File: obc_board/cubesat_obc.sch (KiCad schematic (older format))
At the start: 0 parts

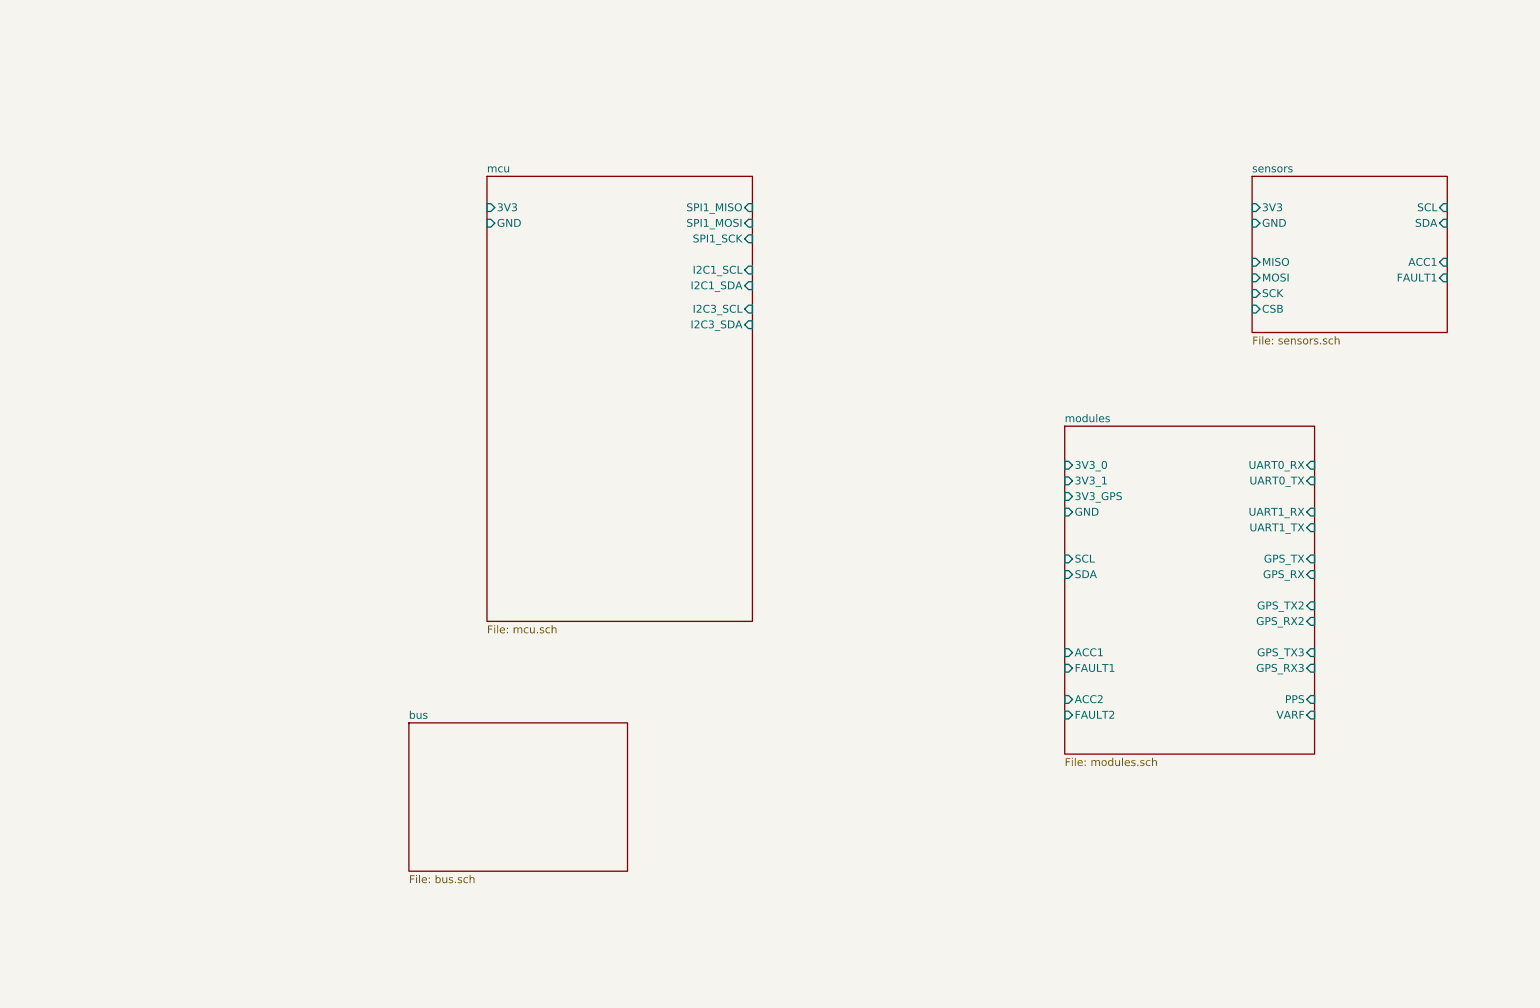
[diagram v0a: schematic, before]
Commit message: add memory
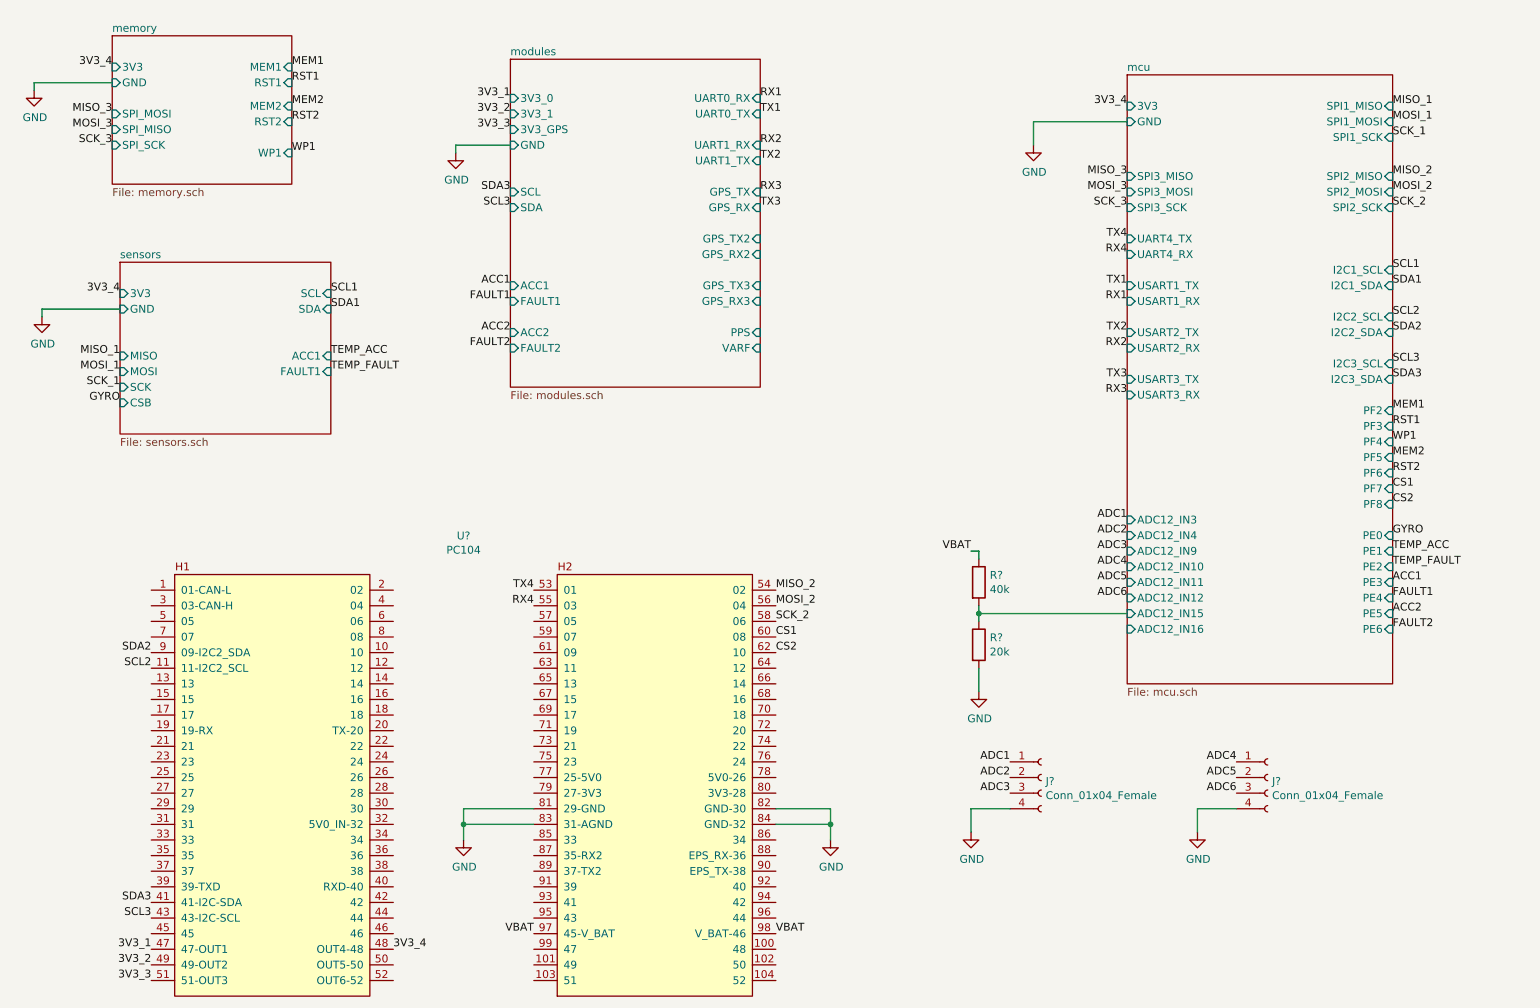
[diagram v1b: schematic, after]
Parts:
- added J? (x2): Conn_01x04_Female, symbol Connector:Conn_01x04_Female
- added R?: 40k, symbol Device:R
- added R?: 20k, symbol Device:R
- added U?: PC104, symbol cubesat_obc_lib:PC104
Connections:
- new net 3V3_1: U?.47 (47-OUT1)
- new net 3V3_2: U?.49 (49-OUT2)
- new net 3V3_3: U?.51 (51-OUT3)
- new net 3V3_4: U?.48 (OUT4-48)
- new net ADC1: J?.1 (Pin_1)
- new net ADC2: J?.2 (Pin_2)
- new net ADC3: J?.3 (Pin_3)
- new net ADC4: J?.1 (Pin_1)
- new net ADC5: J?.2 (Pin_2)
- new net ADC6: J?.3 (Pin_3)
- new net CS1: U?.60 (08)
- new net CS2: U?.62 (10)
- new net GND: J?.4 (Pin_4), J?.4 (Pin_4), R?.2, U?.81 (29-GND), U?.82 (GND-30), U?.83 (31-AGND), U?.84 (GND-32)
- new net MISO_2: U?.54 (02)
- new net MOSI_2: U?.56 (04)
- new net RX4: U?.55 (03)
- new net SCK_2: U?.58 (06)
- new net SCL2: U?.11 (11-I2C2_SCL)
- new net SCL3: U?.43 (43-I2C-SCL)
- new net SDA2: U?.9 (09-I2C2_SDA)
- new net SDA3: U?.41 (41-I2C-SDA)
- new net TX4: U?.53 (01)
- new net VBAT: R?.1, U?.97 (45-V_BAT), U?.98 (V_BAT-46)
- new net mcu/ADC12_IN15: R?.1, R?.2

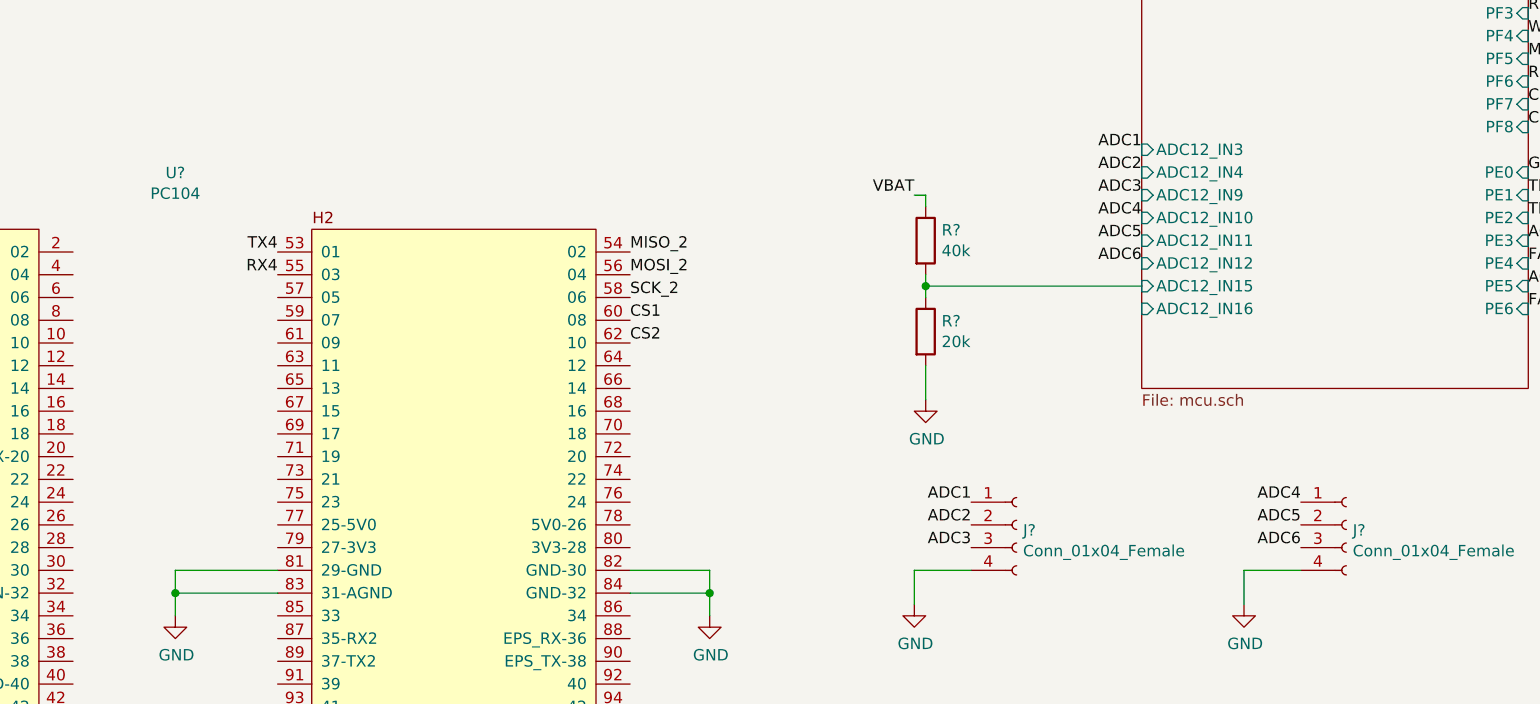
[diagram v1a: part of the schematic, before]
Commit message: updated footprints
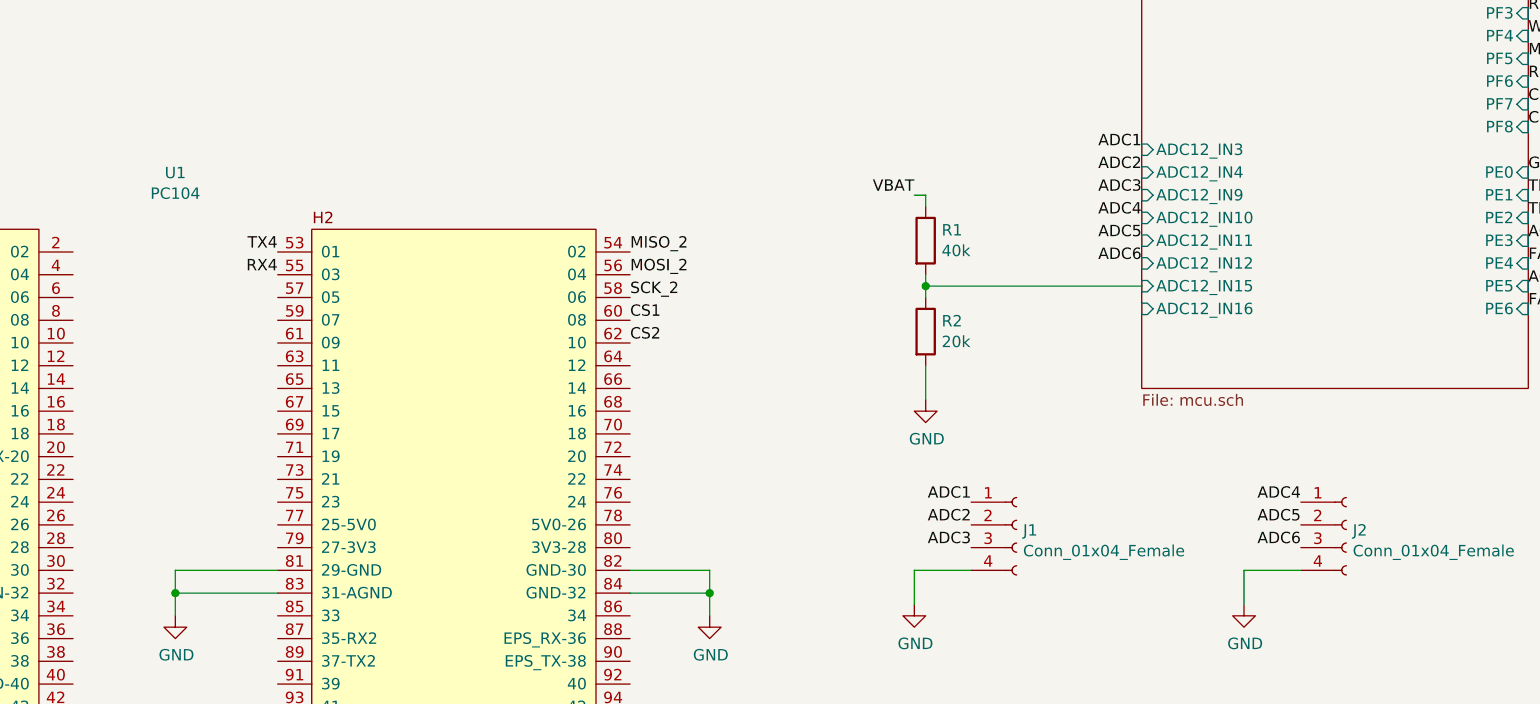
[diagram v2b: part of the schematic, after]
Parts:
- U1: renamed from U?; footprint (none) -> cubesat_obc:PC104-Standard; Digikey Part Number (none) -> 609-10153302-20111LF-ND
- gave numbers to parts that had none: 4
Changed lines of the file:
@@
 $EndDescr
 $Comp
-L power:GND #PWR?
+L power:GND #PWR0101
 U 1 1 5F33CD00
 P 7350 1750
-F 0 "#PWR?" H 7350 1500 50  0001 C CNN
+F 0 "#PWR0101" H 7350 1500 50  0001 C CNN
 F 1 "GND" H 7355 1577 50  0000 C CNN
 F 2 "" H 7350 1750 50  0001 C CNN
@@
 	7350 1750 7350 1600
 $Comp
-L power:GND #PWR?
+L power:GND #PWR0102
 U 1 1 5F33D036
 P 6050 6200
-F 0 "#PWR?" H 6050 5950 50  0001 C CNN
+F 0 "#PWR0102" H 6050 5950 50  0001 C CNN
 F 1 "GND" H 6055 6027 50  0000 C CNN
 F 2 "" H 6050 6200 50  0001 C CNN
@@
 	6050 6100 6050 6000
 $Comp
-L power:GND #PWR?
+L power:GND #PWR0103
 U 1 1 5F33D67B
 P 3700 6200
-F 0 "#PWR?" H 3700 5950 50  0001 C CNN
+F 0 "#PWR0103" H 3700 5950 50  0001 C CNN
 F 1 "GND" H 3705 6027 50  0000 C CNN
 F 2 "" H 3700 6200 50  0001 C CNN
@@
 	3700 6100 3700 6000
 $Comp
-L power:GND #PWR?
+L power:GND #PWR0104
 U 1 1 5F33E025
 P 3650 1800
-F 0 "#PWR?" H 3650 1550 50  0001 C CNN
+F 0 "#PWR0104" H 3650 1550 50  0001 C CNN
 F 1 "GND" H 3655 1627 50  0000 C CNN
 F 2 "" H 3650 1800 50  0001 C CNN
@@
 	3650 1750 3650 1800
 $Comp
-L power:GND #PWR?
+L power:GND #PWR0105
 U 1 1 5F33EB7E
 P 1000 2850
-F 0 "#PWR?" H 1000 2600 50  0001 C CNN
+F 0 "#PWR0105" H 1000 2600 50  0001 C CNN
 F 1 "GND" H 1005 2677 50  0000 C CNN
 F 2 "" H 1000 2850 50  0001 C CNN
@@
 3V3_4
 $Comp
-L cubesat_obc_lib:PC104 U?
+L cubesat_obc_lib:PC104 U1
 U 1 1 5F3402F4
 P 3700 5800
-F 0 "U?" H 3700 7348 50  0000 C CNN
+F 0 "U1" H 3700 7348 50  0000 C CNN
 F 1 "PC104" H 3700 7257 50  0000 C CNN
-F 2 "" H 2600 6600 50  0001 C CNN
-F 3 "" H 2600 6600 50  0001 C CNN
+F 2 "cubesat_obc:PC104-Standard" H 2600 6600 50  0001 C CNN
+F 3 "https://cdn.amphenol-icc.com/media/wysiwyg/files/drawing/10153302.pdf" H 2600 6600 50  0001 C CNN
+F 4 "	609-10153302-20111LF-ND" H 3700 5800 50  0001 C CNN "Digikey Part Number"
 	1    3700 5800
 	1    0    0    -1
@@
 RST2
 $Comp
-L power:GND #PWR?
+L power:GND #PWR0106
 U 1 1 5F5192B7
 P 950 1400
-F 0 "#PWR?" H 950 1150 50  0001 C CNN
+F 0 "#PWR0106" H 950 1150 50  0001 C CNN
 F 1 "GND" H 955 1227 50  0000 C CNN
 F 2 "" H 950 1400 50  0001 C CNN
@@
 CS2
 $Comp
-L Connector:Conn_01x04_Female J?
+L Connector:Conn_01x04_Female J1
 U 1 1 5F6F0159
 P 7400 5800
-F 0 "J?" H 7428 5776 50  0000 L CNN
+F 0 "J1" H 7428 5776 50  0000 L CNN
 F 1 "Conn_01x04_Female" H 7428 5685 50  0000 L CNN
 F 2 "" H 7400 5800 50  0001 C CNN
@@
 ADC3
 $Comp
-L power:GND #PWR?
+L power:GND #PWR0107
 U 1 1 5F6F2A66
 P 6950 6150
-F 0 "#PWR?" H 6950 5900 50  0001 C CNN
+F 0 "#PWR0107" H 6950 5900 50  0001 C CNN
 F 1 "GND" H 6955 5977 50  0000 C CNN
 F 2 "" H 6950 6150 50  0001 C CNN
@@
 	6950 6000 7200 6000
 $Comp
-L Connector:Conn_01x04_Female J?
+L Connector:Conn_01x04_Female J2
 U 1 1 5F6F5054
 P 8850 5800
-F 0 "J?" H 8878 5776 50  0000 L CNN
+F 0 "J2" H 8878 5776 50  0000 L CNN
 F 1 "Conn_01x04_Female" H 8878 5685 50  0000 L CNN
 F 2 "" H 8850 5800 50  0001 C CNN
@@
 $EndComp
 $Comp
-L power:GND #PWR?
+L power:GND #PWR0108
 U 1 1 5F6F505D
 P 8400 6150
-F 0 "#PWR?" H 8400 5900 50  0001 C CNN
+F 0 "#PWR0108" H 8400 5900 50  0001 C CNN
 F 1 "GND" H 8405 5977 50  0000 C CNN
 F 2 "" H 8400 6150 50  0001 C CNN
@@
 ADC6
 $Comp
-L Device:R R?
+L Device:R R1
 U 1 1 5F6F647B
 P 7000 4550
-F 0 "R?" H 7070 4596 50  0000 L CNN
+F 0 "R1" H 7070 4596 50  0000 L CNN
 F 1 "40k" H 7070 4505 50  0000 L CNN
 F 2 "" V 6930 4550 50  0001 C CNN
@@
 $EndComp
 $Comp
-L Device:R R?
+L Device:R R2
 U 1 1 5F6F758C
 P 7000 4950
-F 0 "R?" H 7070 4996 50  0000 L CNN
+F 0 "R2" H 7070 4996 50  0000 L CNN
 F 1 "20k" H 7070 4905 50  0000 L CNN
 F 2 "" V 6930 4950 50  0001 C CNN
@@
 	7000 4700 7000 4750
 $Comp
-L power:GND #PWR?
+L power:GND #PWR0109
 U 1 1 5F6FA8AC
 P 7000 5250
-F 0 "#PWR?" H 7000 5000 50  0001 C CNN
+F 0 "#PWR0109" H 7000 5000 50  0001 C CNN
 F 1 "GND" H 7005 5077 50  0000 C CNN
 F 2 "" H 7000 5250 50  0001 C CNN

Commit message: footprints
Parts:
- J1, J2: footprint (none) -> Connector_Molex:Molex_PicoBlade_53398-0471_1x04-1MP_P1.25mm_Vertical; Digikey Part Number (none) -> WM7608CT-ND
- R1: footprint (none) -> Resistor_SMD:R_0603_1608Metric; Digikey Part Number (none) -> PAT40KACT-ND
- R2: footprint (none) -> Resistor_SMD:R_0603_1608Metric; Digikey Part Number (none) -> 764-1399-1-ND
- U1: Digikey Part Number 609-10153302-20111LF-ND -> (none)
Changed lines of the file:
@@
 F 1 "PC104" H 3700 7257 50  0000 C CNN
 F 2 "cubesat_obc:PC104-Standard" H 2600 6600 50  0001 C CNN
-F 3 "https://cdn.amphenol-icc.com/media/wysiwyg/files/drawing/10153302.pdf" H 2600 6600 50  0001 C CNN
-F 4 "	609-10153302-20111LF-ND" H 3700 5800 50  0001 C CNN "Digikey Part Number"
+F 3 "" H 2600 6600 50  0001 C CNN
+F 4 "" H 3700 5800 50  0001 C CNN "Digikey Part Number"
 	1    3700 5800
 	1    0    0    -1
@@
 F 0 "J1" H 7428 5776 50  0000 L CNN
 F 1 "Conn_01x04_Female" H 7428 5685 50  0000 L CNN
-F 2 "" H 7400 5800 50  0001 C CNN
-F 3 "~" H 7400 5800 50  0001 C CNN
+F 2 "Connector_Molex:Molex_PicoBlade_53398-0471_1x04-1MP_P1.25mm_Vertical" H 7400 5800 50  0001 C CNN
+F 3 "https://www.molex.com/pdm_docs/sd/533980471_sd.pdf" H 7400 5800 50  0001 C CNN
+F 4 "	WM7608CT-ND" H 7400 5800 50  0001 C CNN "Digikey Part Number"
 	1    7400 5800
 	1    0    0    -1
@@
 F 0 "J2" H 8878 5776 50  0000 L CNN
 F 1 "Conn_01x04_Female" H 8878 5685 50  0000 L CNN
-F 2 "" H 8850 5800 50  0001 C CNN
-F 3 "~" H 8850 5800 50  0001 C CNN
+F 2 "Connector_Molex:Molex_PicoBlade_53398-0471_1x04-1MP_P1.25mm_Vertical" H 8850 5800 50  0001 C CNN
+F 3 "https://www.molex.com/pdm_docs/sd/533980471_sd.pdf" H 8850 5800 50  0001 C CNN
+F 4 "	WM7608CT-ND" H 8850 5800 50  0001 C CNN "Digikey Part Number"
 	1    8850 5800
 	1    0    0    -1
@@
 F 0 "R1" H 7070 4596 50  0000 L CNN
 F 1 "40k" H 7070 4505 50  0000 L CNN
-F 2 "" V 6930 4550 50  0001 C CNN
-F 3 "~" H 7000 4550 50  0001 C CNN
+F 2 "Resistor_SMD:R_0603_1608Metric" V 6930 4550 50  0001 C CNN
+F 3 "http://www.vishay.com/docs/60024/pat.pdf~" H 7000 4550 50  0001 C CNN
+F 4 "PAT40KACT-ND" H 7000 4550 50  0001 C CNN "Digikey Part Number"
 	1    7000 4550
 	1    0    0    -1
@@
 F 0 "R2" H 7070 4996 50  0000 L CNN
 F 1 "20k" H 7070 4905 50  0000 L CNN
-F 2 "" V 6930 4950 50  0001 C CNN
-F 3 "~" H 7000 4950 50  0001 C CNN
+F 2 "Resistor_SMD:R_0603_1608Metric" V 6930 4950 50  0001 C CNN
+F 3 "http://www.vishay.com/docs/60026/ptn.pdf~" H 7000 4950 50  0001 C CNN
+F 4 "764-1399-1-ND" H 7000 4950 50  0001 C CNN "Digikey Part Number"
 	1    7000 4950
 	1    0    0    -1

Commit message: expose more ios
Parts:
- removed U1: PC104, cubesat_obc:PC104-Standard, symbol cubesat_obc_lib:PC104
- added H? (x4): MountingHole, symbol Mechanical:MountingHole
- added J? (x3): Conn_01x03_Female, symbol Connector:Conn_01x03_Female
- J1, J2: Digikey Part Number WM7608CT-ND -> WM7608CT-ND
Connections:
- net GND: now also J?.3 (Pin_3), J?.3 (Pin_3), J?.3 (Pin_3)
- net RX2: now also J?.2 (Pin_2)
- net RX3: now also J?.2 (Pin_2)
- net RX4: now also J?.2 (Pin_2)
- net TX2: now also J?.1 (Pin_1)
- net TX3: now also J?.1 (Pin_1)
- net TX4: now also J?.1 (Pin_1)
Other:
- moved on the sheet: J1, J2, R1, R2

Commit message: footprints
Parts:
- added J?: Conn_01x03_Female, symbol Connector:Conn_01x03_Female
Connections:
- net GND: now also J?.3 (Pin_3)
- net SCL2: now also J?.2 (Pin_2)
- net SDA2: now also J?.1 (Pin_1)
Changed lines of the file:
@@
 F47 "ADC12_IN9" I L 8300 4050 50
 F48 "ADC12_IN10" I L 8300 4150 50
+F49 "3V3_P" I L 8300 1400 50
+F50 "PG6" I L 8300 3300 50
+F51 "PG7" I L 8300 3400 50
+F52 "PG8" I L 8300 3500 50
 $EndSheet
 $Sheet
@@
 Text Label 5050 5100 2    50   ~ 0
 RX2
+$Comp
+L Connector:Conn_01x03_Female J?
+U 1 1 5F5B1828
+P 6700 3350
+F 0 "J?" H 6728 3376 50  0000 L CNN
+F 1 "Conn_01x03_Female" H 6728 3285 50  0000 L CNN
+F 2 "" H 6700 3350 50  0001 C CNN
+F 3 "~" H 6700 3350 50  0001 C CNN
+	1    6700 3350
+	1    0    0    -1
+$EndComp
+$Comp
+L power:GND #PWR?
+U 1 1 5F5B182E
+P 6250 3600
+F 0 "#PWR?" H 6250 3350 50  0001 C CNN
+F 1 "GND" H 6255 3427 50  0000 C CNN
+F 2 "" H 6250 3600 50  0001 C CNN
+F 3 "" H 6250 3600 50  0001 C CNN
+	1    6250 3600
+	1    0    0    -1
+$EndComp
+Wire Wire Line
+	6250 3600 6250 3450
+Wire Wire Line
+	6250 3450 6500 3450
+Text Label 6500 3250 2    50   ~ 0
+SDA2
+Text Label 6500 3350 2    50   ~ 0
+SCL2
+Text Label 8300 1400 2    50   ~ 0
+3V3_P
 $EndSCHEMATC

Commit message: pcb layout
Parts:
- removed J? (x4): Conn_01x03_Female, symbol Connector:Conn_01x03_Female
- added J1, J2, J3, J4: Conn_01x04_Female, Connector_Molex:Molex_PicoBlade_53261-0471_1x04-1MP_P1.25mm_Horizontal, symbol Connector:Conn_01x04_Female
- added J5: Conn_01x05_Female, Connector_Molex:Molex_PicoBlade_53261-0571_1x05-1MP_P1.25mm_Horizontal, symbol Connector:Conn_01x05_Female
- H1, H2, H3, H4: renamed from H?; footprint (none) -> MountingHole:MountingHole_3.2mm_M3_DIN965_Pad
- J6: renamed from J1; footprint Connector_Molex:Molex_PicoBlade_53398-0471_1x04-1MP_P1.25mm_Vertical -> Connector_Molex:Molex_PicoBlade_53261-0471_1x04-1MP_P1.25mm_Horizontal; Digikey Part Number WM7608CT-ND -> WM7622CT-ND
- J7: renamed from J2; footprint Connector_Molex:Molex_PicoBlade_53398-0471_1x04-1MP_P1.25mm_Vertical -> Connector_Molex:Molex_PicoBlade_53261-0471_1x04-1MP_P1.25mm_Horizontal; Digikey Part Number WM7608CT-ND -> WM7622CT-ND
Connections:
- net GND: now also J1.4 (Pin_4), J2.4 (Pin_4), J3.4 (Pin_4), J4.4 (Pin_4), J5.5 (Pin_5)
- net MISO_2: now also J5.3 (Pin_3)
- net MOSI_2: now also J5.2 (Pin_2)
- net RX1: now also J1.3 (Pin_3)
- net RX2: now also J2.3 (Pin_3)
- net RX3: now also J3.3 (Pin_3)
- net RX4: now also J4.3 (Pin_3)
- net SCK_2: now also J5.1 (Pin_1)
- net TX1: now also J1.2 (Pin_2)
- net TX2: now also J2.2 (Pin_2)
- net TX3: now also J3.2 (Pin_2)
- net TX4: now also J4.2 (Pin_2)
- new net VCC: J1.1 (Pin_1), J2.1 (Pin_1), J3.1 (Pin_1), J4.1 (Pin_1)
